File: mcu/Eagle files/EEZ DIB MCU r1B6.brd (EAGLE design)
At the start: 139.5 x 70 mm, 181 parts, among them IC1 CD74HC4050PWR, IC10 TPD4E001DRLR, IC11 TSC2007IPW, IC12 TPD4E001DRLR, IC13 DP83848CVV/NOPB, IC14 TPD4E001DRLR, IC2 STM32F769IGT6, IC3 LD1117ADT33TR, IC4 TPD4E001DRLR, IC5 IS42S16400J, IC6 AT24C256C-SSHL-B, IC7 TPS2051BDBVR, IC8 TPS61169DCKR, IC9 TPD4E001DRLR, J1 503398-1892, J2 67803-8020, Q1 N.C., Q2 2N7002, SW1 TL1100CF160Q, SW2 PEC16-2215F-S0024, X1 DS1024-2*20R0, X2 DS1013-16SSIB1, X3 1844249, X4 N.C., X5 LMJTAB881243M-L, Y1 25MHz, Y2 XTAL016178-85SMX

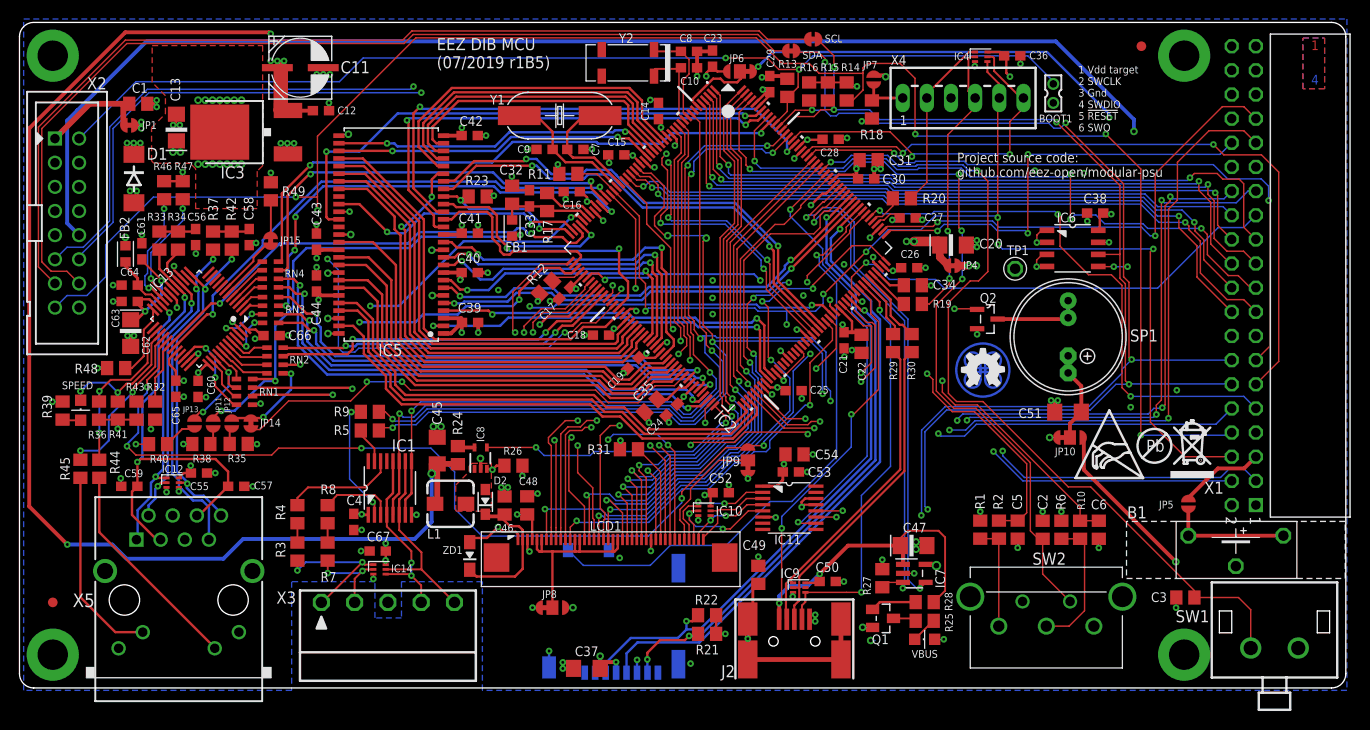
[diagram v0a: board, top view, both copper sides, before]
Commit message: MCU reset issue, encoder moved
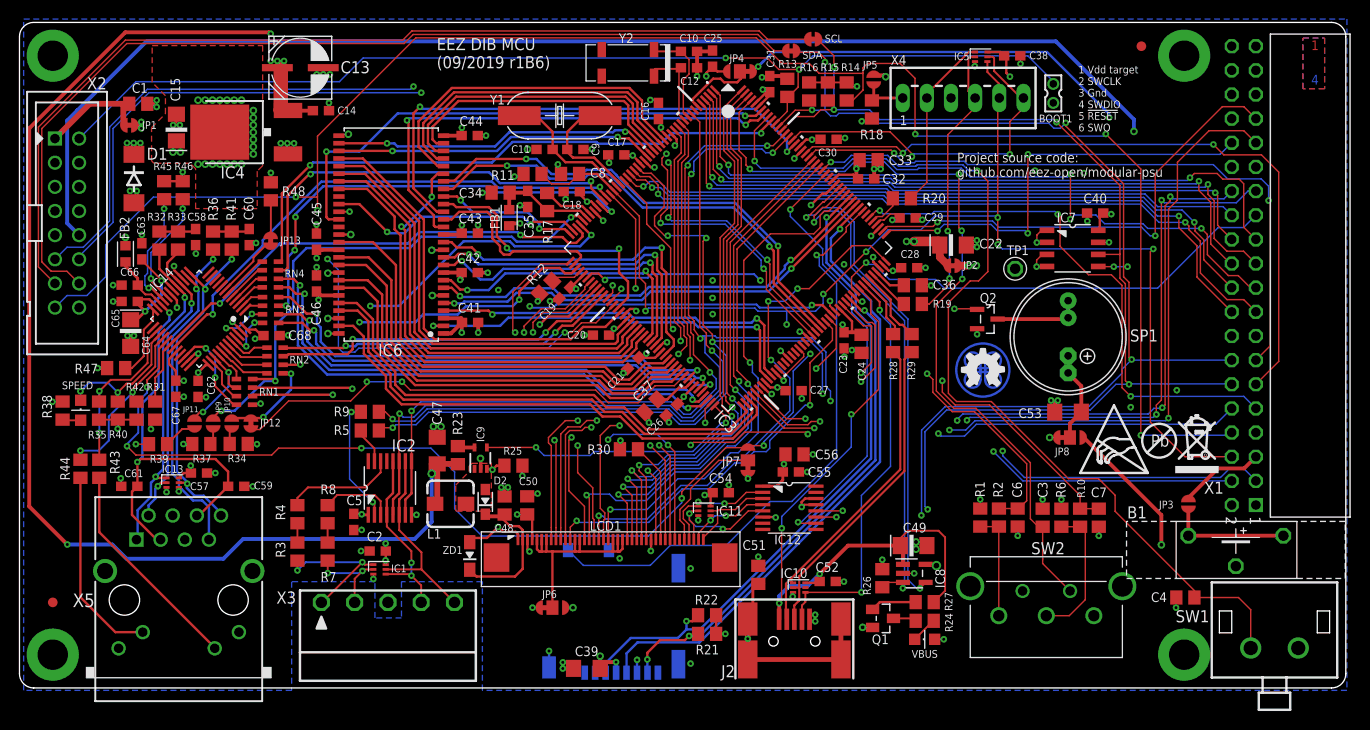
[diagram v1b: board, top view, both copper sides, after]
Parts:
- removed JP14, JP15: JP2-NOCUT, EEZ_Lib1:JP2-NOCUT
- removed R49: 2K2, rcl:R0805
- added C68: 100n, rcl:C0603
- added JP2: JP2-NOCUT, EEZ_Lib1:JP2-NOCUT
- added JP3: JP2-CUT, EEZ_Lib1:JP2-CUT
- C11: value EEEFK1V470P -> 18p; device EEZ_Lib1:CAPAE660X610N -> rcl:C0603
- C12: value 100n -> 4p7
- C13: value 4u7 -> EEEFK1V470P; device EEZ_Lib1:EC1206 -> EEZ_Lib1:CAPAE660X610N
- C15: value 100n -> 4u7; device rcl:C0603 -> EEZ_Lib1:EC1206
- C2: value 10n -> N.C.; device rcl:C0805 -> rcl:C0603
- C20: value 4u7 -> 100n; device EEZ_Lib1:EC1206 -> rcl:C0603
- C22: value 1u -> 4u7; device rcl:C0805 -> EEZ_Lib1:EC1206
- C23, C52, C55, C67: value N.C. -> 100n
- C24, C33, C56: value 100n -> 1u; device rcl:C0603 -> rcl:C0805
- C25, C38, C57: value 100n -> N.C.
- C31, C32, C46: value 1u -> 100n; device rcl:C0805 -> rcl:C0603
- C34, C48: value 2u2 -> 1u
- C35: value 2u2 -> 100n; device rcl:C0805 -> rcl:C0603
- C36: value N.C. -> 2u2; device rcl:C0603 -> rcl:C0805
- C37: value 4u7 -> 2u2; device rcl:C1206 -> rcl:C0805
- C39, C53: value 100n -> 4u7; device rcl:C0603 -> rcl:C1206
- C4: value 100n -> 10n; device rcl:C0603 -> rcl:C0805
- C45: value 4u7 -> 100n; device rcl:C1206 -> rcl:C0603
- C47: device EEZ_Lib1:EC1206 -> rcl:C1206
- C49: value N.C. -> 4u7; device rcl:C0805 -> EEZ_Lib1:EC1206
- C5: value 10n -> 100n; device rcl:C0805 -> rcl:C0603
- C50: value 100n -> 2u2; device rcl:C0603 -> rcl:C0805
- C51: value 4u7 -> N.C.; device rcl:C1206 -> rcl:C0805
- C54: value 1u -> N.C.; device rcl:C0805 -> rcl:C0603
- C62: value 10u -> 100n; device EEZ_Lib1:EC1206 -> rcl:C0603
- C64: value 100n -> 10u; device rcl:C0603 -> EEZ_Lib1:EC1206
- C7: value 18p -> 10n; device rcl:C0603 -> rcl:C0805
- C8: value 4p7 -> 1n; device rcl:C0603 -> rcl:C0805
- IC1: value CD74HC4050PWR -> TPD4E001DRLR; device EEZ_DIB:PW16 -> EEZ_Lib1:DRL6
- IC11: value TSC2007IPW -> TPD4E001DRLR; device EEZ_Lib1:PW(R-PDSO-G16) -> EEZ_Lib1:DRL6
- IC12: value TPD4E001DRLR -> TSC2007IPW; device EEZ_Lib1:DRL6 -> EEZ_Lib1:PW(R-PDSO-G16)
- IC13: value DP83848CVV/NOPB -> TPD4E001DRLR; device EEZ_Lib1:PT48 -> EEZ_Lib1:DRL6
- IC14: value TPD4E001DRLR -> DP83848CVV/NOPB; device EEZ_Lib1:DRL6 -> EEZ_Lib1:PT48
- IC2: value STM32F769IGT6 -> CD74HC4050PWR; device EEZ_DIB:LQFP-176_24X24MM -> EEZ_DIB:PW16
- IC3: value LD1117ADT33TR -> STM32F769IGT6; device v-reg:DPACK -> EEZ_DIB:LQFP-176_24X24MM
- IC4: value TPD4E001DRLR -> LD1117ADT33TR; device EEZ_Lib1:DRL6 -> v-reg:DPACK
- IC5: value IS42S16400J -> TPD4E001DRLR; device EEZ_Lib1:TSOPII-54 -> EEZ_Lib1:DRL6
- IC6: value AT24C256C-SSHL-B -> IS42S16400J; device EEZ_Lib1:SOIC127P600X173-8N -> EEZ_Lib1:TSOPII-54
- IC7: value TPS2051BDBVR -> AT24C256C-SSHL-B; device EEZ_Lib1:DBV5 -> EEZ_Lib1:SOIC127P600X173-8N
- IC8: value TPS61169DCKR -> TPS2051BDBVR; device EEZ_Lib1:DCK5 -> EEZ_Lib1:DBV5
- IC9: value TPD4E001DRLR -> TPS61169DCKR; device EEZ_Lib1:DRL6 -> EEZ_Lib1:DCK5
- JP10, JP9: value JP3-CUT -> JP2-CUT; device EEZ_Lib1:JP3-CUT -> EEZ_Lib1:JP2-CUT
- JP12, JP13: value JP2-CUT -> JP2-NOCUT; device EEZ_Lib1:JP2-CUT -> EEZ_Lib1:JP2-NOCUT
- JP4: value JP2-NOCUT -> JP3-CUT; device EEZ_Lib1:JP2-NOCUT -> EEZ_Lib1:JP3-CUT
- JP7: value JP2-CUT -> JP3-CUT; device EEZ_Lib1:JP2-CUT -> EEZ_Lib1:JP3-CUT
- R11: value 10K -> 4K7
- R23, R25: value N.C. -> 10R
- R24, R26: value 10R -> N.C.
- R28: value N.C. -> 22R
- R30: value 22R -> N.C.
- R31: value 10K -> 1K5
- R32: value 1K5 -> 49R9
- R34, R37, R42: value 49R9 -> 2K2
- R36, R41: value 2K2 -> 49R9
- R38: value 2K2 -> N.C.
- R39: value N.C. -> 2K2
- R43: value 2K2 -> 220R
- R45: value 220R -> 2K2
- R47: value 2K2 -> 4K87
- R48: value 4K87 -> 2K2
- moved JP10 88.2 mm to (17.3, 27.8), turned to 270 degrees
- moved C4 87.8 mm to (117.6, 9.51), turned to 0 degrees
- moved IC4 78.1 mm to (18.4, 58.5), turned to 90 degrees
- moved IC6 71.7 mm to (34.1, 47.7), turned to 180 degrees
- moved C2 70.0 mm to (32.7, 14.4), turned to 180 degrees
- moved C5 69.8 mm to (30.2, 17.5), turned to 270 degrees
- moved C7 67.3 mm to (108.5, 17.9), turned to 270 degrees
- moved C56 67.0 mm to (76.5, 24.6), turned to 180 degrees
- moved C40 66.1 mm to (108.1, 49.9)
- moved IC12 64.9 mm to (76.0, 18.9)
- moved IC5 64.8 mm to (96.2, 66.4), turned to 0 degrees
- moved C55 62.3 mm to (76.1, 22.7), turned to 180 degrees
- moved JP6 59.7 mm to (51.1, 8.45), turned to 0 degrees
- moved JP8 57.3 mm to (105.5, 26.3)
- moved JP9 56.4 mm to (15.4, 27.8), turned to 270 degrees
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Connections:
- removed net LTDC_B2: IC2.150, LCD1.23
- removed net LTDC_R2: IC2.139, LCD1.7
- net !FAULT: now also IC3.58; no longer IC2.58
- net !RESET: now also C8.1, IC14.29, IC3.31, IC5.4, JP7.NO; no longer IC13.29, IC2.31, IC4.4, JP9.NO
- net !USB_OTG_FS_OC: now also IC3.146, IC8.3, R26.1; no longer IC2.146, IC7.3, R27.1
- net +3V3: now also C15.+, C38.1, C40.2, C45.1, C46.1, C5.1, C50.1, C55.2, C56.2, C57.1, C67.1, C68.1, IC11.6, IC12.1, IC13.6, IC14.32, IC14.48, IC2.1, IC4.4, IC5.6, IC6.1, IC6.14, IC6.27, IC6.3, IC6.43, IC6.49, IC6.9, IC7.8, JP2.2, JP5.1, JP6.NO, JP8.NC, R26.2, R30.2, R35.1, R38.1, R42.1, R45.1, R48.1; no longer C13.+, C36.1, C37.1, C38.2, C4.1, C40.1, C48.1, C52.2, C53.2, C55.1, C65.1, C66.1, IC1.1, IC10.6, IC11.1, IC12.6, IC13.32, IC13.48, IC3.4, IC4.6, IC5.1, IC5.14, IC5.27, IC5.3, IC5.43, IC5.49, IC5.9, IC6.8, JP10.NC, JP4.2, JP7.1, JP8.NO, R23.1, R27.2, R32.2, R36.1, R41.1, R43.1, R47.1, R49.1
- net +3V3(A): now also C61.2, C66.1, IC14.22; no longer C57.2, C64.1, IC13.22
- net +5V: now also C13.1, C14.1, C2.1, C47.1, IC1.6, IC4.3, IC8.5, JP8.NO, R23.1; no longer C11.1, C12.1, C45.1, C67.1, IC14.6, IC3.3, IC7.5, JP10.NO, R24.1
- net +VAUX: now also JP3.2; no longer JP5.2
- net BOOT0: now also IC3.166; no longer IC2.166
- net BYPASS_REG: now also IC3.48; no longer IC2.48
- net DAC_OUT1: now also IC3.50; no longer IC2.50
- net DIN2: now also IC3.8; no longer IC2.8
- net DOUT2: now also IC2.7, IC2.9, IC3.163; no longer IC1.7, IC1.9, IC2.163
- net ENC_A: now also C6.2, IC3.119; no longer C5.2, IC2.119
- net ENC_B: now also C7.1, IC3.120; no longer C6.1, IC2.120
- net ENC_SW: now also C3.2, IC3.173; no longer C2.2, IC2.173
- net ETH_COL: now also IC3.47; no longer IC2.47
- net ETH_CRS: now also IC3.40, JP9.1; no longer IC2.40, JP11.1
- net ETH_MDC: now also IC14.31, IC3.33; no longer IC13.31, IC2.33
- net ETH_MDIO: now also IC14.30, IC3.42, R31.1; no longer IC13.30, IC2.42, R32.1
- net ETH_RXD0: now also IC3.54; no longer IC2.54
- net ETH_RXD1: now also IC3.55; no longer IC2.55
- net ETH_RXD2: now also IC3.83; no longer IC2.83
- net ETH_RXD3: now also IC3.84; no longer IC2.84
- net ETH_RX_CLK: now also IC3.41; no longer IC2.41
- net ETH_RX_DV: now also IC3.53; no longer IC2.53
- net ETH_RX_ER: now also JP10.1; no longer JP14.1
- net ETH_RX_ERR: now also IC3.79, JP12.2; no longer IC2.79, JP14.2
- net ETH_TXD0: now also IC3.85; no longer IC2.85
- net ETH_TXD1: now also IC3.86; no longer IC2.86
- net ETH_TXD2: now also IC3.34; no longer IC2.34
- net ETH_TXD3: now also IC3.167; no longer IC2.167
- net ETH_TX_CLK: now also IC3.35; no longer IC2.35
- net ETH_TX_EN: now also IC3.80; no longer IC2.80
- net FMC_A0: now also IC3.16, IC6.23; no longer IC2.16, IC5.23
- net FMC_A1: now also IC3.17, IC6.24; no longer IC2.17, IC5.24
- net FMC_A10: now also IC3.66, IC6.22; no longer IC2.66, IC5.22
- net FMC_A11: now also IC3.67, IC6.35; no longer IC2.67, IC5.35
- net FMC_A2: now also IC3.18, IC6.25; no longer IC2.18, IC5.25
- net FMC_A3: now also IC3.19, IC6.26; no longer IC2.19, IC5.26
- net FMC_A4: now also IC3.20, IC6.29; no longer IC2.20, IC5.29
- net FMC_A5: now also IC3.21, IC6.30; no longer IC2.21, IC5.30
- net FMC_A6: now also IC3.60, IC6.31; no longer IC2.60, IC5.31
- net FMC_A7: now also IC3.63, IC6.32; no longer IC2.63, IC5.32
- net FMC_A8: now also IC3.64, IC6.33; no longer IC2.64, IC5.33
- net FMC_A9: now also IC3.65, IC6.34; no longer IC2.65, IC5.34
- net FMC_BA0: now also IC3.112, IC6.20; no longer IC2.112, IC5.20
- net FMC_BA1: now also IC3.113, IC6.21; no longer IC2.113, IC5.21
- net FMC_D0: now also IC3.97, IC6.2; no longer IC2.97, IC5.2
- net FMC_D1: now also IC3.98, IC6.4; no longer IC2.98, IC5.4
- net FMC_D10: now also IC3.76, IC6.45; no longer IC2.76, IC5.45
- net FMC_D11: now also IC3.77, IC6.47; no longer IC2.77, IC5.47
- net FMC_D12: now also IC3.78, IC6.48; no longer IC2.78, IC5.48
- net FMC_D13: now also IC3.89, IC6.50; no longer IC2.89, IC5.50
- net FMC_D14: now also IC3.90, IC6.51; no longer IC2.90, IC5.51
- net FMC_D15: now also IC3.91, IC6.53; no longer IC2.91, IC5.53
- net FMC_D2: now also IC3.142, IC6.5; no longer IC2.142, IC5.5
- net FMC_D3: now also IC3.143, IC6.7; no longer IC2.143, IC5.7
- net FMC_D4: now also IC3.68, IC6.8; no longer IC2.68, IC5.8
- net FMC_D5: now also IC3.69, IC6.10; no longer IC2.69, IC5.10
- net FMC_D6: now also IC3.70, IC6.11; no longer IC2.70, IC5.11
- net FMC_D7: now also IC3.73, IC6.13; no longer IC2.73, IC5.13
- net FMC_D8: now also IC3.74, IC6.42; no longer IC2.74, IC5.42
- net FMC_D9: now also IC3.75, IC6.44; no longer IC2.75, IC5.44
- net FMC_NBL0: now also IC3.169, IC6.15; no longer IC2.169, IC5.15
- net FMC_NBL1: now also IC3.170, IC6.39; no longer IC2.170, IC5.39
- net FMC_SDCKE0: now also IC3.43, IC6.37; no longer IC2.43, IC5.37
- net FMC_SDCLK: now also IC3.116, IC6.38; no longer IC2.116, IC5.38
- net FMC_SDNCAS: now also IC3.160, IC6.17; no longer IC2.160, IC5.17
- net FMC_SDNE0: now also IC3.44, IC6.19; no longer IC2.44, IC5.19, R23.2
- net FMC_SDNRAS: now also IC3.59, IC6.18; no longer IC2.59, IC5.18
- net FMC_SDNWE: now also IC3.46, IC6.16; no longer IC2.46, IC5.16
- net GND: now also C11.1, C13.2, C15.-, C2.2, C20.2, C22.-, C38.2, C4.1, C40.1, C47.2, C49.-, C5.2, C50.2, C51.2, C55.1, C56.1, C57.2, C6.1, C61.1, C62.2, C64.-, C68.2, C7.2, IC1.3, IC11.3, IC12.13, IC12.14, IC12.6, IC13.3, IC14.15, IC14.19, IC14.35, IC14.36, IC14.47, IC2.8, IC3.103, IC3.109, IC3.117, IC3.130, IC3.135, IC3.14, IC3.148, IC3.158, IC3.22, IC3.37, IC3.61, IC3.71, IC3.95, IC4.1, IC5.3, IC6.12, IC6.28, IC6.41, IC6.46, IC6.52, IC6.54, IC6.6, IC7.1, IC7.3, IC7.4, IC7.7, IC9.2, JP6.NC, JP7.NC, R25.2, R34.1, R37.1, R47.1; no longer C11.2, C13.-, C15.2, C2.1, C20.-, C22.2, C38.1, C4.2, C40.2, C47.-, C49.2, C5.1, C50.1, C51.1, C55.2, C56.2, C57.1, C6.2, C61.2, C62.-, C64.2, C7.1, C8.2, IC1.8, IC11.13, IC11.14, IC11.6, IC12.3, IC13.15, IC13.19, IC13.35, IC13.36, IC13.47, IC14.3, IC2.103, IC2.109, IC2.117, IC2.130, IC2.135, IC2.14, IC2.148, IC2.158, IC2.22, IC2.37, IC2.61, IC2.71, IC2.95, IC3.1, IC4.3, IC5.12, IC5.28, IC5.41, IC5.46, IC5.52, IC5.54, IC5.6, IC6.1, IC6.2, IC6.3, IC6.4, IC6.7, IC9.3, JP8.NC, JP9.NC, R26.2, R35.1, R38.1, R48.1
- net I2C1_SCL: now also IC12.12, IC3.164, IC7.6; no longer IC11.12, IC2.164, IC6.6
- net I2C1_SDA: now also IC12.11, IC3.165, IC7.5; no longer IC11.11, IC2.165, IC6.5
- net IRQ_TOUCH: now also IC12.10, IC3.151; no longer IC11.10, IC2.151
- net LCD_DISP: now also R30.1; no longer R31.1
- net LED_ACT: now also IC14.26, R35.2, R43.2; no longer IC13.26, R36.2, R44.2
- net LED_LINK: now also IC14.28, R42.2, R44.2; no longer IC13.28, R43.2, R45.2
- net LED_SPEED: now also IC14.27, R40.2; no longer IC13.27, R41.2
- net LTDC_B3: now also IC3.154; no longer IC2.154
- net LTDC_B4: now also IC3.155; no longer IC2.155
- net LTDC_B5: now also IC3.174; no longer IC2.174
- net LTDC_B6: now also IC3.175; no longer IC2.175
- net LTDC_B7: now also IC3.176; no longer IC2.176
- net LTDC_CLK: now also IC3.115; no longer IC2.115
- net LTDC_DE: now also IC3.28; no longer IC2.28
- net LTDC_G2: now also IC3.52; no longer IC2.52
- net LTDC_G3: now also IC3.153; no longer IC2.153
- net LTDC_G4: now also IC3.45; no longer IC2.45
- net LTDC_G5: now also IC3.132; no longer IC2.132
- net LTDC_G6: now also IC3.13; no longer IC2.13
- net LTDC_G7: now also IC3.145; no longer IC2.145
- net LTDC_HSYNC: now also IC3.12; no longer IC2.12
- net LTDC_R3: now also IC3.56; no longer IC2.56
- net LTDC_R4: now also IC3.51; no longer IC2.51
- net LTDC_R5: now also IC3.32; no longer IC2.32
- net LTDC_R6: now also IC3.57; no longer IC2.57
- net LTDC_R7: now also IC3.114; no longer IC2.114
- net LTDC_VSYNC: now also IC3.11; no longer IC2.11
- net MCLK_25: now also IC3.122; no longer IC2.122
- net N$1: now also IC14.1; no longer IC13.1
- net N$10: now also IC14.2; no longer IC13.2
- net N$101: now also R38.2; no longer R39.2
- net N$102: now also C60.1, R36.1, R41.2; no longer C58.1, R37.1, R42.2
- net N$11: now also IC14.39, JP11.2; no longer IC13.39, JP13.2
- net N$12: now also IC14.38; no longer IC13.38
- net N$14: now also IC1.2; no longer IC14.2
- net N$15: now also IC14.3; no longer IC13.3
- net N$16: now also R24.1; no longer R25.1
- net N$17: now also IC14.4; no longer IC13.4
- net N$178: now also IC3.100, IC3.106; no longer IC2.100, IC2.106
- net N$19: now also R27.2; no longer R28.2
- net N$2: now also R24.2; no longer R25.2
- net N$20: now also JP3.1, JP4.NC; no longer JP5.1, JP6.NC
- net N$21: now also IC14.5; no longer IC13.5
- net N$22: now also IC14.34; no longer IC13.34
- net N$23: now also JP11.1, R39.2; no longer JP13.1, R40.2
- net N$24: now also JP7.COM; no longer JP9.COM
- net N$25: now also JP9.2, R37.2; no longer JP11.2, R38.2
- net N$26: now also JP10.2, R34.2; no longer JP12.2, R35.2
- net N$27: now also IC14.7, JP13.2; no longer IC13.7, JP15.2
- net N$28: now also JP13.1, R48.2; no longer JP15.1, R49.2
- net N$29: now also IC14.6; no longer IC13.6
- net N$3: now also C58.1, R32.1, R33.2; no longer C56.1, R33.1, R34.2
- net N$30: now also IC9.5, R23.2; no longer IC8.5, R24.2
- net N$31: now also IC14.46; no longer IC13.46
- net N$32: now also IC14.45; no longer IC13.45
- net N$33: now also IC14.42; no longer IC13.42
- net N$34: now also IC14.44; no longer IC13.44
- net N$35: now also IC14.43; no longer IC13.43
- net N$36: now also IC14.41; no longer IC13.41
- net N$37: now also IC14.40; no longer IC13.40
- net N$4: now also JP6.COM, LCD1.23, LCD1.7; no longer JP8.COM
- net N$42: now also IC2.15; no longer IC1.15
- net N$43: now also IC2.2; no longer IC1.2
- net N$46: now also IC2.14; no longer IC1.14
- net N$47: now also IC2.3; no longer IC1.3
- net N$48: now also IC2.12, IC2.4; no longer IC1.12, IC14.4
- net N$49: now also IC1.5, IC2.10, IC2.6; no longer IC1.10, IC1.6, IC14.5
- net N$51: now also JP5.2; no longer JP7.2
- net N$52: now also C53.2, JP8.COM; no longer C51.2, JP10.COM
- net N$6: now also IC1.1; no longer IC14.1
- net N$8: now also R43.1; no longer R44.1
- net N$9: now also R44.1; no longer R45.1
- net N$97: now also IC14.24, R47.2; no longer IC13.24, R48.2
- net N$98: now also IC14.21, R45.2; no longer IC13.21, R46.2
- net N$99: now also IC14.20, R46.2; no longer IC13.20, R47.2
- net OE_SYNC: now also IC3.94; no longer IC2.94
- net PE: now also C51.1; no longer C49.1
- net PFBOUT: now also C62.1, C64.+, C65.1, IC14.18, IC14.23, IC14.37; no longer C60.1, C61.1, C62.+, IC13.18, IC13.23, IC13.37
- net PWR_DIRECT: now also IC3.110; no longer IC2.110
- net PWR_SSTART: now also IC3.111; no longer IC2.111
- net RCC_OSC32_IN: now also C10.1, IC3.9; no longer C8.1, IC2.9
- net RCC_OSC32_OUT: now also C12.1, IC3.10; no longer C10.1, IC2.10
- net RCC_OSC_IN: now also C9.2, IC3.29; no longer C7.2, IC2.29
- net RCC_OSC_OUT: now also C11.2, IC3.30; no longer C9.2, IC2.30
- net RD+: now also IC13.4, IC14.14, R36.2; no longer IC12.4, IC13.14, R37.2
- net RD-: now also IC13.5, IC14.13, R41.1; no longer IC12.5, IC13.13, R42.1
- net SDMMC1_CK: now also IC3.141; no longer IC2.141
- net SDMMC1_CMD: now also IC3.144; no longer IC2.144
- net SDMMC1_D0: now also IC3.121; no longer IC2.121
- net SD_DETECT: now also IC3.140; no longer IC2.140
- net SPI2_CLK: now also IC3.133; no longer IC2.133
- net SPI2_CSA: now also IC3.93; no longer IC2.93
- net SPI2_CSB: now also IC3.92; no longer IC2.92
- net SPI2_IRQ: now also IC3.123; no longer IC2.123
- net SPI2_MISO: now also IC3.87; no longer IC2.87
- net SPI2_MOSI: now also IC3.134; no longer IC2.134
- net SPI4_CLK: now also IC3.1; no longer IC2.1
- net SPI4_CSA: now also IC3.2; no longer IC2.2
- net SPI4_CSB: now also IC3.3; no longer IC2.3
- net SPI4_IRQ: now also IC3.168; no longer IC2.168
- net SPI4_MISO: now also IC3.4; no longer IC2.4
- net SPI4_MOSI: now also IC3.5; no longer IC2.5
- net SPI5_CLK: now also IC3.25; no longer IC2.25
- net SPI5_CSA: now also IC3.157; no longer IC2.157
- net SPI5_CSB: now also IC3.156; no longer IC2.156
- net SPI5_IRQ: now also IC3.138; no longer IC2.138
- net SPI5_MISO: now also IC3.26; no longer IC2.26
- net SPI5_MOSI: now also IC3.27; no longer IC2.27
- net SW_WLED: now also IC9.1; no longer IC8.1
- net SYS_JTCK-SWCLK: now also IC3.137; no longer IC2.137
- net SYS_JTDO-SWO: now also IC3.161, IC5.5; no longer IC2.161, IC4.5
- net SYS_JTMS-SWDIO: now also IC3.128; no longer IC2.128
- net TCK: now also IC5.1; no longer IC4.1
- net TD+: now also IC13.1, IC14.17, R32.2; no longer IC12.1, IC13.17, R33.2
- net TD-: now also IC13.2, IC14.16, R33.1; no longer IC12.2, IC13.16, R34.1
- net TFT_BRIGHTNESS: now also IC3.88, IC9.4; no longer IC2.88, IC8.4
- net TMS: now also IC5.2; no longer IC4.2
- net UART_RX/DIN1: now also IC3.24; no longer IC2.24
- net UART_TX/DOUT1: now also IC2.11, IC2.5, IC3.162; no longer IC1.11, IC1.5, IC2.162
- net USB_D_N: now also IC10.1, R28.1; no longer IC9.1, R29.1
- net USB_D_P: now also IC10.2, R29.1; no longer IC9.2, R30.1
- net USB_OTG_FS_D_N: now also IC3.126, R28.2; no longer IC2.126, R29.2
- net USB_OTG_FS_D_P: now also IC3.127, R29.2; no longer IC2.127, R30.2
- net USB_OTG_FS_ID: now also IC10.4, IC3.125; no longer IC2.125, IC9.4
- net USB_OTG_FS_PSO: now also IC3.147, IC8.4; no longer IC2.147, IC7.4
- net USB_OTG_FS_VBUS: now also C49.+, C52.2, IC10.6, IC3.124, IC8.1, R27.1; no longer C47.+, C50.2, IC2.124, IC7.1, IC9.6, R28.1
- net USER_SW: now also C4.2, IC3.152; no longer C3.2, IC2.152
- net VBAT: now also IC3.6, JP4.COM; no longer IC2.6, JP6.COM
- net VCAP1: now also C37.1, IC3.81; no longer C35.1, IC2.81
- net VCAP2: now also C36.1, IC3.129; no longer C34.1, IC2.129
- net VDD: now also C20.1, C22.+, C32.1, C33.1, C8.2, IC3.118, IC3.131, IC3.136, IC3.149, IC3.15, IC3.159, IC3.171, IC3.172, IC3.23, IC3.36, IC3.49, IC3.62, IC3.72, IC3.82, IC3.96, IC3.99, JP2.1, JP4.NO; no longer C14.1, C15.1, C20.+, C22.1, IC2.118, IC2.131, IC2.136, IC2.149, IC2.15, IC2.159, IC2.171, IC2.172, IC2.23, IC2.36, IC2.49, IC2.62, IC2.72, IC2.82, IC2.96, IC2.99, JP4.1, JP6.NO
- net VDDA: now also C34.1, C35.1, IC3.39; no longer C32.1, C33.1, IC2.39
- net VLED+: now also C48.1; no longer C46.1
- net VLED-: now also IC9.3, R25.1; no longer IC8.3, R26.1
- net VREF+: now also IC3.38; no longer IC2.38
- net XL: now also IC12.4; no longer IC10.4
- net XR: now also IC11.1, IC12.2; no longer IC10.1, IC11.2
- net YD: now also IC11.2, IC12.5; no longer IC10.2, IC11.5
- net YU: now also IC11.5, IC12.3; no longer IC10.5, IC11.3
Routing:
- net LTDC_R2: track 61.6 -> 0.00 mm, vias 5 -> 0
- net LTDC_B2: track 55.7 -> 0.00 mm, vias 2 -> 0
- net VDD: track 64.1 -> 70.8 mm, vias 20 -> 21
- net !RESET: track 233.8 -> 238.4 mm
- net N$4: track 21.7 -> 24.8 mm
- net +5V: track 248.8 -> 246.6 mm
- net GND: track 143.1 -> 141.1 mm, vias 147 -> 148
- net ENC_A: track 39.9 -> 38.6 mm
- net +3V3: track 92.8 -> 91.6 mm, vias 54 -> 59
- net LTDC_G5: track 56.6 -> 55.4 mm
- net VDDA: track 10.2 -> 11.3 mm
- net ENC_SW: track 85.0 -> 83.9 mm
- net FMC_SDNE0: track 16.4 -> 15.3 mm
- net USER_SW: track 89.9 -> 90.9 mm
- net FMC_SDCKE0: track 28.1 -> 27.5 mm
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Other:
- board text added: "EEZ DIB MCU (09/2019 r1B6)"
- board text removed: "EEZ DIB MCU (07/2019 r1B5)"

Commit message: MCU IC2 label added
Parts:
- R30: value N.C. -> 10K
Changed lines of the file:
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@@
 <layers>
 <layer number="1" name="Top" color="11" fill="1" visible="yes" active="yes"/>
-<layer number="2" name="Gnd" color="2" fill="1" visible="no" active="yes"/>
+<layer number="2" name="Gnd" color="2" fill="1" visible="yes" active="yes"/>
 <layer number="3" name="Route3" color="4" fill="3" visible="no" active="no"/>
 <layer number="4" name="Route4" color="1" fill="4" visible="no" active="no"/>
@@
 <layer number="21" name="tPlace" color="7" fill="1" visible="yes" active="yes"/>
 <layer number="22" name="bPlace" color="13" fill="1" visible="no" active="yes"/>
-<layer number="23" name="tOrigins" color="15" fill="1" visible="yes" active="yes"/>
+<layer number="23" name="tOrigins" color="15" fill="1" visible="no" active="yes"/>
 <layer number="24" name="bOrigins" color="15" fill="1" visible="no" active="yes"/>
 <layer number="25" name="tNames" color="7" fill="1" visible="yes" active="yes"/>
@@
 <layer number="49" name="Reference" color="7" fill="1" visible="no" active="yes"/>
 <layer number="50" name="dxf" color="7" fill="1" visible="no" active="no"/>
-<layer number="51" name="tDocu" color="14" fill="1" visible="yes" active="yes"/>
+<layer number="51" name="tDocu" color="14" fill="1" visible="no" active="yes"/>
 <layer number="52" name="bDocu" color="7" fill="1" visible="no" active="yes"/>
 <layer number="53" name="tGND_GNDA" color="7" fill="9" visible="no" active="no"/>
@@
 <attribute name="VALUE" x="44.3624" y="16.5657" size="0.6096" layer="27" ratio="10" rot="R90"/>
 </element>
-<element name="R30" library="rcl" package="R0805" value="N.C." x="59.1058" y="25.1079" smashed="yes" rot="R180">
+<element name="R30" library="rcl" package="R0805" value="10K" x="59.1058" y="25.1079" smashed="yes" rot="R180">
 <attribute name="NAME" x="57.1881" y="25.6159" size="1.016" layer="25" ratio="10" rot="R180"/>
 <attribute name="VALUE" x="57.9882" y="24.6253" size="1.016" layer="27" ratio="10"/>

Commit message: clean up Gerber files
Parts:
- X3: value 1844249 -> 691322110005
- moved C15 7.82 mm to (8.20, 66.0), turned to 180 degrees
- moved C1 1.40 mm to (6.44, 62.4), turned to 90 degrees
- moved C53 1.37 mm to (103.9, 29.0)
- moved JP2 0.19 mm to (93.2, 44.6)
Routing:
- net N$52: track 9.66 -> 8.66 mm
- net +3V3: track 91.6 -> 91.1 mm, vias 59 -> 57
- added copper zone on layer 16, net +3V3
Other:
- board text added: "EEZ DIB MCU (12/2019 r1B6)"
- board text removed: "EEZ DIB MCU (09/2019 r1B6)"
